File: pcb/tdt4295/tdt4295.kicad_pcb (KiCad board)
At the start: 6 copper layers, 184 parts, among them J101 ARM 20 Pin Debug Header, J102 MCU USART1 Header, J103 DM1AA-SF-PEJ(21), J104 MCU GPIO Header, J301 FPGA__debug, J501 618015330923, J502 FPGA GPIO, P201 690-005-299-043, U101 EFM32GG12B810F1024GQ64, U102 COM-09032 Joystick, U103 COM-09032 Joystick, U201 PHDMI2AB4, U202 TPS54294, U203 TPS54294, U301 S25FL127SABMFV101, U302 SOIC_W1T2G_ONS, U303 XC7A100T-FTG256-tdt4295, U501 SOIC_W1T2G_ONS, U502 SOIC_W1T2G_ONS, U503 SOIC_W1T2G_ONS, U504 SOIC_W1T2G_ONS, U601 DSC1001AL5-100.0000, Y101 48MHz

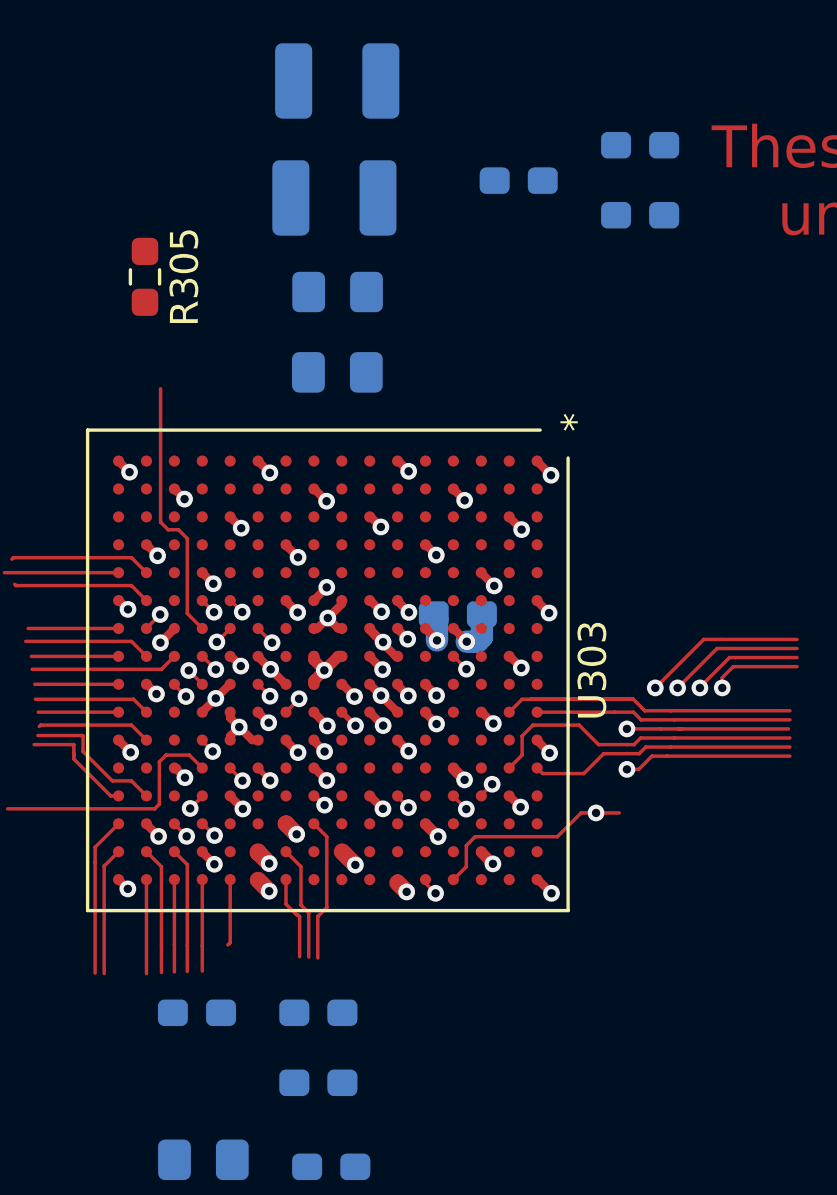
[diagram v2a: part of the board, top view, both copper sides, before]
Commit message: power zones on FPGA
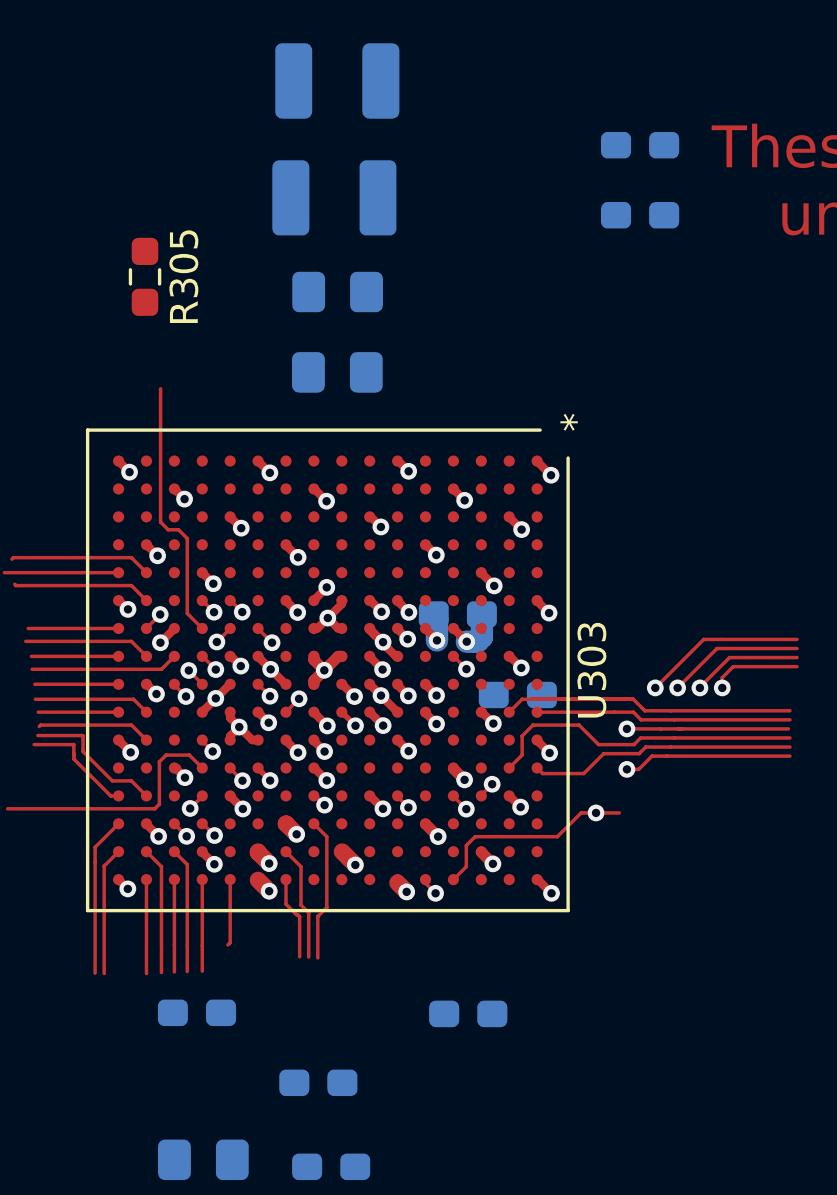
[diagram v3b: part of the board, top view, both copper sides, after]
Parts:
- moved C404 18.4 mm to (98.2, 75.2)
- moved C608 5.37 mm to (96.4, 86.6), turned to 180 degrees
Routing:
- net +1V0: track 5.57 -> 15.2 mm
- net +1V8: track 94.9 -> 102.9 mm
- added copper zone on +PWR, net +1V0
- added copper zone on +PWR, net +1V8

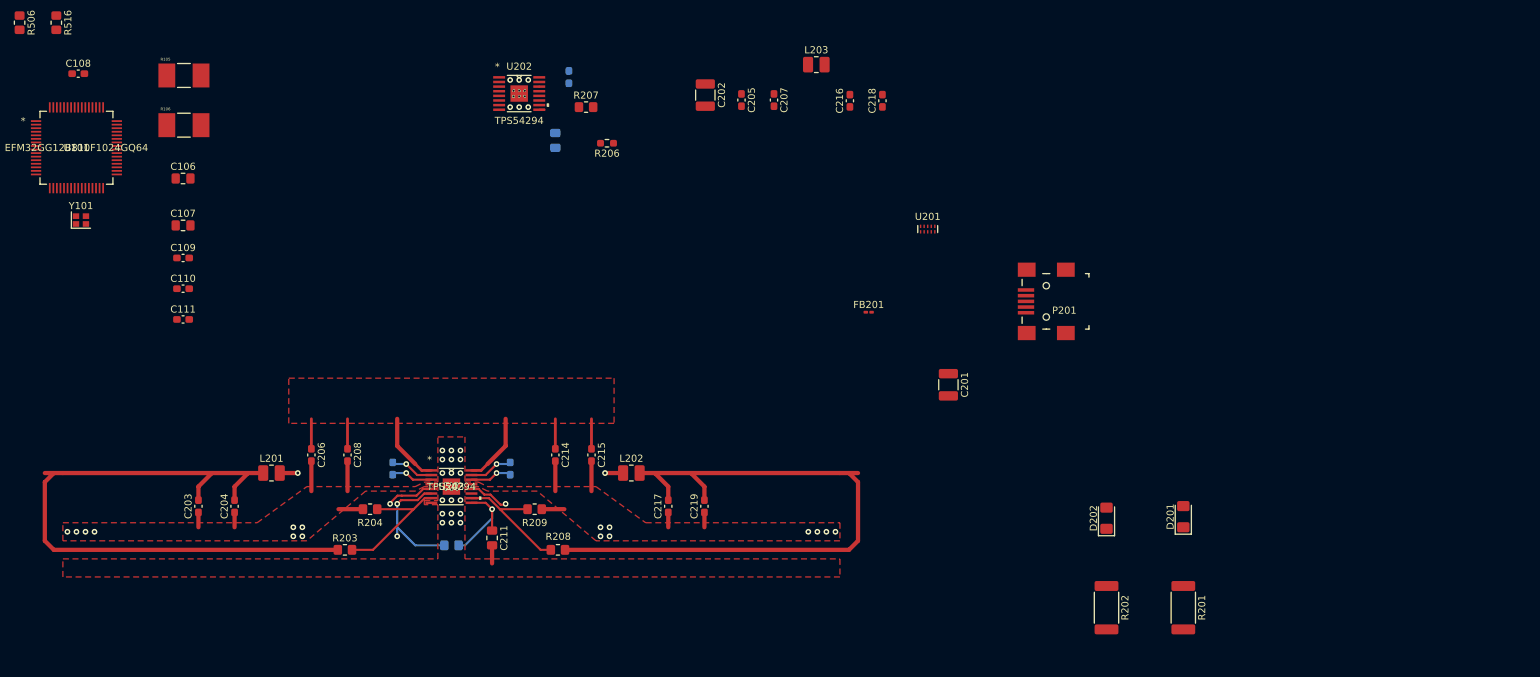
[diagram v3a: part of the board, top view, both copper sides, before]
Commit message: Finish routing voltage regulators
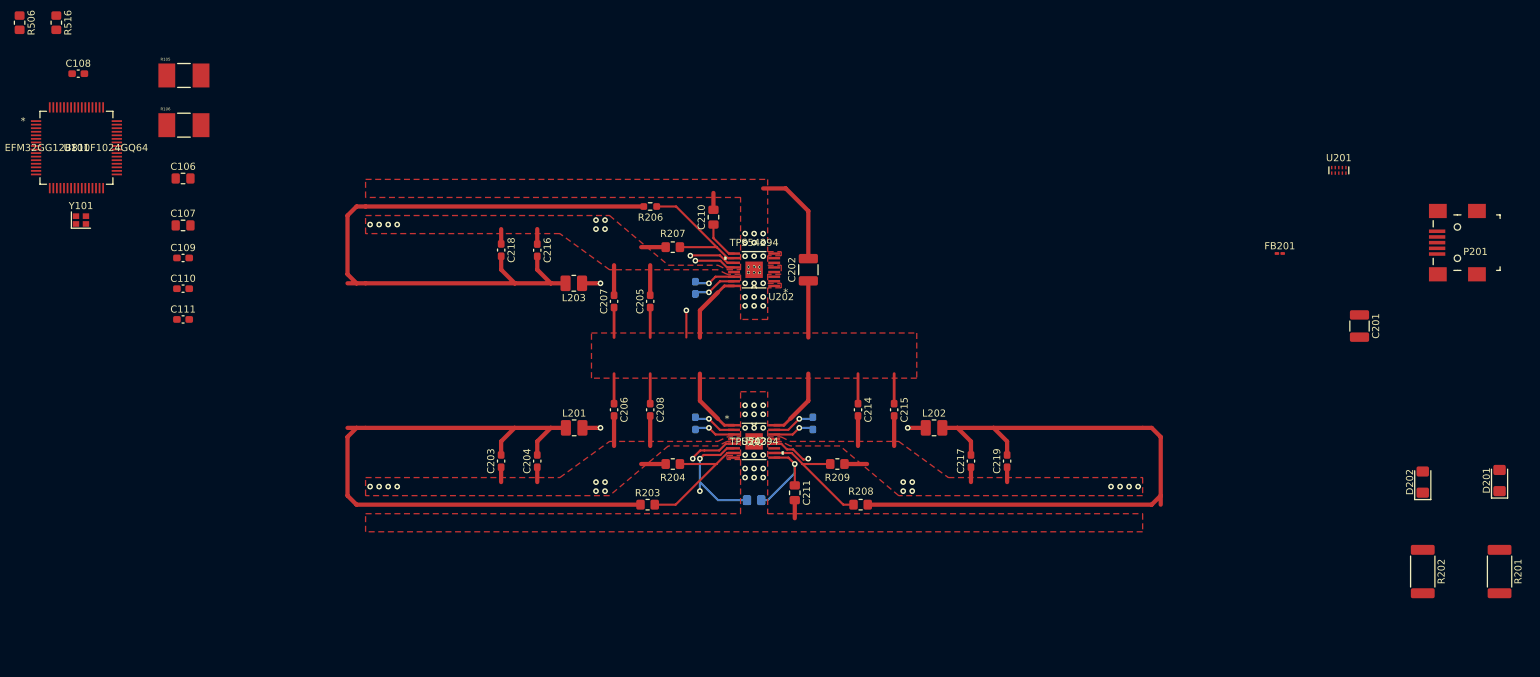
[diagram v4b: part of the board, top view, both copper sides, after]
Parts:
- C210: moved to F.Cu
- moved C201 58.4 mm to (356.9, 82.2)
- moved FB201 58.4 mm to (345.7, 72.0)
- moved P201 58.4 mm to (370.6, 70.5)
- moved U201 58.4 mm to (354.0, 60.3)
- moved C218 57.5 mm to (236.2, 71.5), turned to 270 degrees
- moved C216 48.7 mm to (241.3, 71.6), turned to 270 degrees
- moved L203 45.9 mm to (246.4, 76.2), turned to 180 degrees
- moved D201 44.7 mm to (376.6, 103.9)
- moved D202 44.7 mm to (365.8, 104.1)
- moved R201 44.7 mm to (376.6, 116.7)
- moved R202 44.7 mm to (365.8, 116.7)
- moved C204 43.0 mm to (241.3, 101.2)
- moved C208 43.0 mm to (257.2, 94.0)
- moved C211 43.0 mm to (277.5, 105.6)
- moved C212 43.0 mm to (280.0, 95.9)
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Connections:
- U202 pad V: (no net) -> GND
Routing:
- net +1V0: track 15.2 -> 107.2 mm
- net +5V: track 36.9 -> 80.7 mm, vias 0 -> 2
- net R1_PG: track 6.73 -> 43.1 mm, vias 1 -> 2
- net GND: track 91.7 -> 124.5 mm, vias 82 -> 102
- net Net-(C213-Pad1): track 0.02 -> 23.8 mm, vias 0 -> 2
- net Net-(R206-Pad2): track 0.00 -> 19.1 mm
- net Net-(C213-Pad2): track 0.00 -> 6.17 mm, vias 0 -> 1
- net Net-(C210-Pad1): track 0.73 -> 5.70 mm

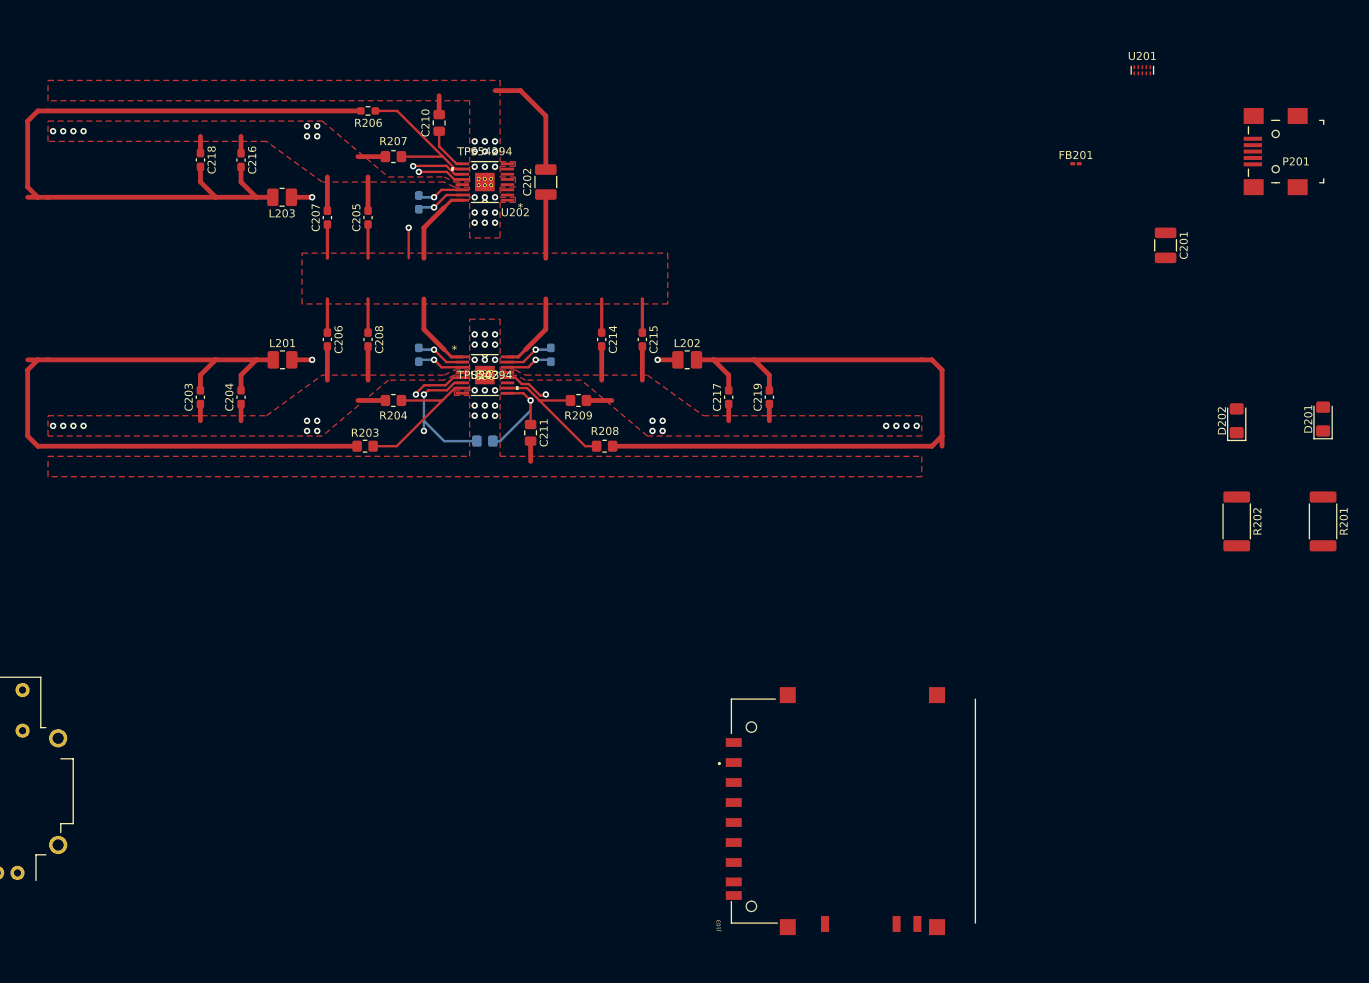
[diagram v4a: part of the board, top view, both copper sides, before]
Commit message: finish routing power input
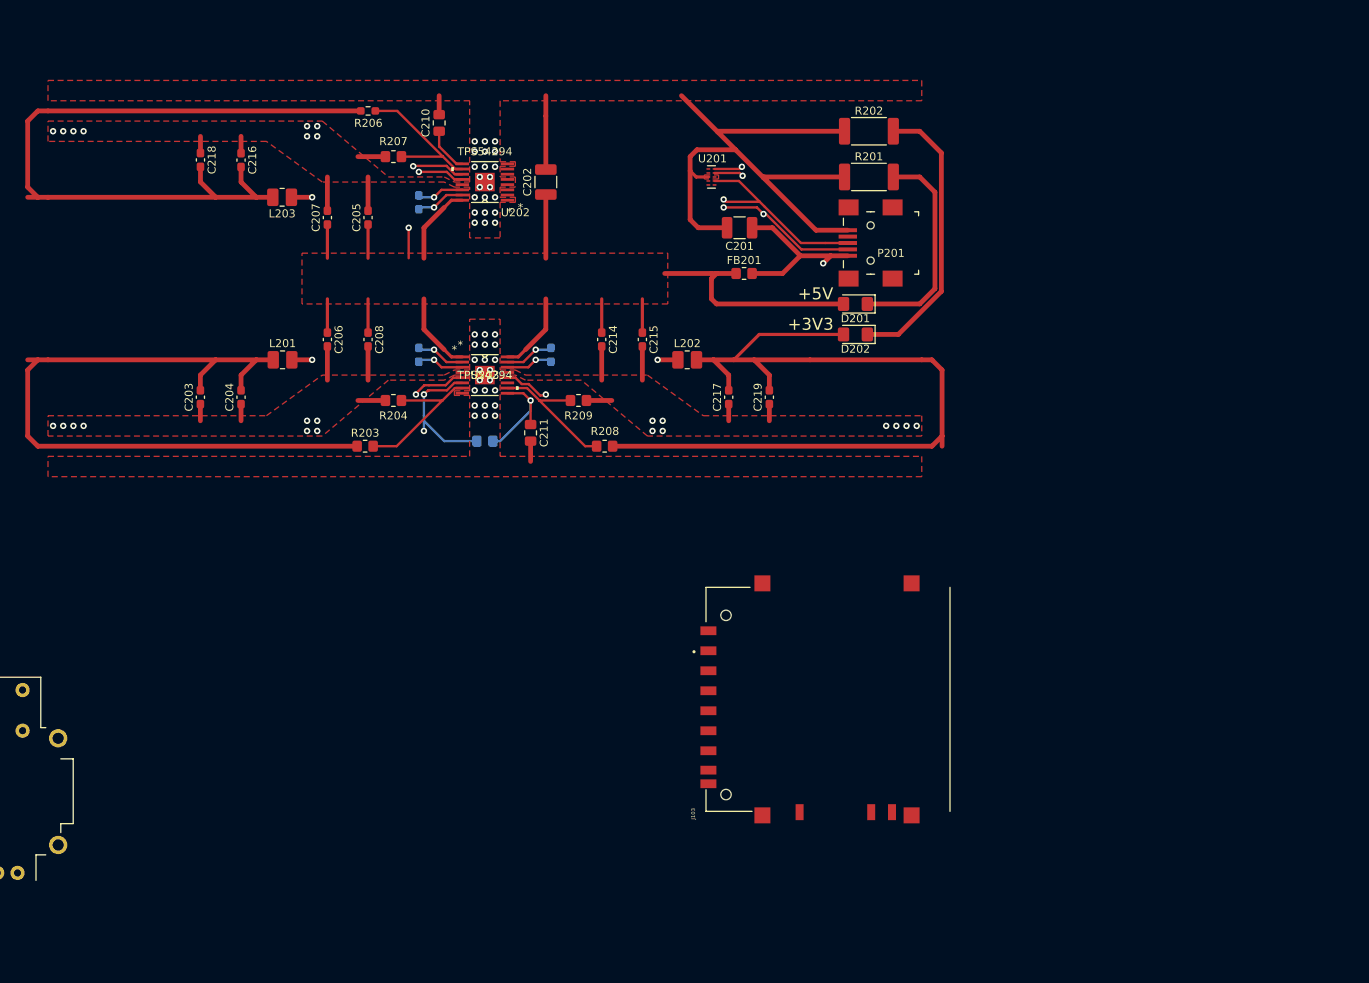
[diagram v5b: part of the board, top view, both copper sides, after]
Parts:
- FB201: footprint Resistor_SMD:R_0201_0603Metric_Pad0.64x0.40mm_HandSolder -> Resistor_SMD:R_0805_2012Metric_Pad1.20x1.40mm_HandSolder
- U302, U501, U502, U503, U504: value SOIC_W1T2G_ONS -> NUP4114UCW1T2G
- moved R201 71.2 mm to (319.8, 73.7), turned to 180 degrees
- moved R202 67.0 mm to (319.8, 67.9), turned to 180 degrees
- moved D201 60.2 mm to (318.1, 89.5), turned to 180 degrees
- moved U201 55.5 mm to (300.1, 73.7), turned to 270 degrees
- moved C201 53.3 mm to (303.6, 80.0), turned to 180 degrees
- moved P201 51.9 mm to (320.0, 81.9)
- moved D202 48.9 mm to (318.1, 93.3), turned to 180 degrees
- moved FB201 43.7 mm to (304.2, 85.7)
- moved J103 14.3 mm to (314.7, 139.8)
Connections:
- J101 pad 11: (no net) -> Net-(J101-Pad11)
- J101 pad 17: (no net) -> Net-(J101-Pad17)
- J101 pad 19: (no net) -> Net-(J101-Pad19)
- J101 pad 2: (no net) -> Net-(J101-Pad2)
- J101 pad 3: (no net) -> Net-(J101-Pad3)
- J101 pad 5: (no net) -> Net-(J101-Pad5)
- J103 pad 12: (no net) -> Net-(J103-Pad12)
- J103 pad 13: (no net) -> Net-(J103-Pad13)
- J104 pad 5: (no net) -> Net-(J104-Pad5)
- J104 pad 6: (no net) -> Net-(J104-Pad6)
- J301 pad 12: (no net) -> Net-(J301-Pad12)
- J301 pad 14: (no net) -> Net-(J301-Pad14)
- J501 pad 11: (no net) -> Net-(J501-Pad11)
- J501 pad 12: (no net) -> Net-(J501-Pad12)
- J501 pad 15: (no net) -> Net-(J501-Pad15)
- J501 pad 4: (no net) -> Net-(J501-Pad4)
- J501 pad 9: (no net) -> Net-(J501-Pad9)
- P201 pad 4: (no net) -> Net-(P201-Pad4)
- U101 pad 37: (no net) -> Net-(U101-Pad37)
- U101 pad 45: (no net) -> Net-(U101-Pad45)
- U102 pad B1A: (no net) -> Net-(U102-PadB1A)
- U102 pad B2A: (no net) -> Net-(U102-PadB2A)
- U103 pad B1A: (no net) -> Net-(U103-PadB1A)
- U103 pad B2A: (no net) -> Net-(U103-PadB2A)
- U201 pad 10: (no net) -> Net-(U201-Pad10)
- U201 pad 5: (no net) -> Net-(U201-Pad5)
- U201 pad 6: (no net) -> Net-(U201-Pad6)
- U201 pad 7: (no net) -> Net-(U201-Pad7)
- U201 pad 9: (no net) -> Net-(U201-Pad9)
- U202 pad 2: (no net) -> Net-(U202-Pad2)
- U202 pad 3: (no net) -> Net-(U202-Pad3)
- U202 pad 6: (no net) -> Net-(U202-Pad6)
- U202 pad 7: (no net) -> Net-(U202-Pad7)
- U203 pad 11: (no net) -> Net-(U203-Pad11)
- U303 pad A13: (no net) -> Net-(U303-PadA13)
- U303 pad A14: (no net) -> Net-(U303-PadA14)
- U303 pad A15: (no net) -> Net-(U303-PadA15)
- U303 pad A8: (no net) -> Net-(U303-PadA8)
- U303 pad A9: (no net) -> Net-(U303-PadA9)
- U303 pad B11: (no net) -> Net-(U303-PadB11)
- U303 pad B14: (no net) -> Net-(U303-PadB14)
- U303 pad B15: (no net) -> Net-(U303-PadB15)
- U303 pad B16: (no net) -> Net-(U303-PadB16)
- U303 pad B9: (no net) -> Net-(U303-PadB9)
- U303 pad C11: (no net) -> Net-(U303-PadC11)
- U303 pad C12: (no net) -> Net-(U303-PadC12)
- U303 pad C14: (no net) -> Net-(U303-PadC14)
- U303 pad C16: (no net) -> Net-(U303-PadC16)
- U303 pad C8: (no net) -> Net-(U303-PadC8)
- U303 pad C9: (no net) -> Net-(U303-PadC9)
- U303 pad D10: (no net) -> Net-(U303-PadD10)
- U303 pad D11: (no net) -> Net-(U303-PadD11)
- U303 pad D14: (no net) -> Net-(U303-PadD14)
- U303 pad D15: (no net) -> Net-(U303-PadD15)
- U303 pad D9: (no net) -> Net-(U303-PadD9)
- U303 pad E11: (no net) -> Net-(U303-PadE11)
- U303 pad E12: (no net) -> Net-(U303-PadE12)
- U303 pad E13: (no net) -> Net-(U303-PadE13)
- U303 pad E15: (no net) -> Net-(U303-PadE15)
- U303 pad F12: (no net) -> Net-(U303-PadF12)
- U303 pad F14: (no net) -> Net-(U303-PadF14)
- U303 pad F15: (no net) -> Net-(U303-PadF15)
- U303 pad G11: (no net) -> Net-(U303-PadG11)
- U303 pad G12: (no net) -> Net-(U303-PadG12)
- U303 pad G14: (no net) -> Net-(U303-PadG14)
- U303 pad G15: (no net) -> Net-(U303-PadG15)
- U303 pad G16: (no net) -> Net-(U303-PadG16)
- U303 pad H11: (no net) -> Net-(U303-PadH11)
- U303 pad H12: (no net) -> Net-(U303-PadH12)
- U303 pad H13: (no net) -> Net-(U303-PadH13)
- U303 pad H14: (no net) -> Net-(U303-PadH14)
- U303 pad H16: (no net) -> Net-(U303-PadH16)
- U303 pad J15: (no net) -> Net-(U303-PadJ15)
- U303 pad J16: (no net) -> Net-(U303-PadJ16)
- U303 pad K12: (no net) -> Net-(U303-PadK12)
- U303 pad K13: (no net) -> Net-(U303-PadK13)
- U303 pad K7: (no net) -> Net-(U303-PadK7)
- U303 pad K8: (no net) -> Net-(U303-PadK8)
- U303 pad L13: (no net) -> Net-(U303-PadL13)
- U303 pad L14: (no net) -> Net-(U303-PadL14)
- U303 pad M14: (no net) -> Net-(U303-PadM14)
- U303 pad M15: (no net) -> Net-(U303-PadM15)
- U303 pad P10: (no net) -> Net-(U303-PadP10)
- U303 pad P11: (no net) -> Net-(U303-PadP11)
- U303 pad P6: (no net) -> Net-(U303-PadP6)
- U303 pad R12: (no net) -> Net-(U303-PadR12)
- U303 pad T12: (no net) -> Net-(U303-PadT12)
- U501 pad 4: (no net) -> Net-(U501-Pad4)
- U504 pad 4: (no net) -> Net-(U504-Pad4)
- U601 pad 5: (no net) -> Net-(U601-Pad5)
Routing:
- net GND: track 124.5 -> 194.7 mm, vias 102 -> 110
- net Net-(C201-Pad1): track 0.00 -> 40.5 mm, vias 0 -> 2
- net Net-(D202-Pad1): track 0.00 -> 35.9 mm
- net +5V: track 80.7 -> 109.9 mm
- net USB_D-: track 0.00 -> 28.6 mm, vias 0 -> 3
- net Net-(D201-Pad1): track 0.00 -> 27.3 mm
- net USB_D+: track 0.00 -> 24.5 mm, vias 0 -> 1
- net +3V3: track 118.3 -> 133.3 mm
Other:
- board text added: "+3V3"
- board text added: "+5V"

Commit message: assorted minor fixes
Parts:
- moved FB201 2.16 mm to (306.3, 85.7)
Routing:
- net GND: track 194.7 -> 208.7 mm
- net Net-(C201-Pad1): track 40.5 -> 38.3 mm
- net +5V: track 109.9 -> 112.1 mm
